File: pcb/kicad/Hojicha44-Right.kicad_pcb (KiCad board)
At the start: 2 copper layers, 150.5 x 114.6 mm, 54 parts

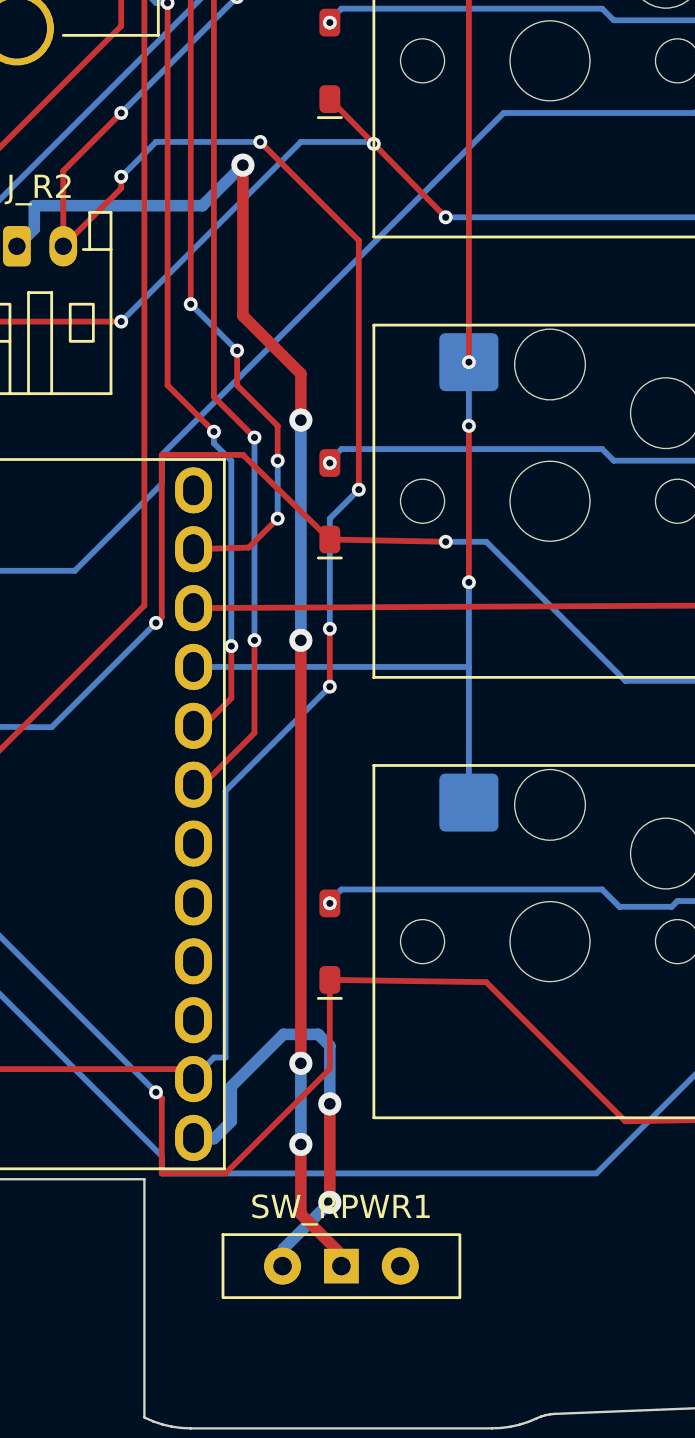
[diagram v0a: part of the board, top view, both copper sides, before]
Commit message: Review round 2: B1 pillar clearance blocker + T4 cover magnets + M2 pwrsw shift + M1 floor ruler + gate hardening
B1 (blocker): tab pillar fuse reached 1.0mm inboard of the rim - solid
case material under the PCB at all 8 stations (board rests ~1.05mm
high, bottom pads unload). Pillar now starts 0.3 outboard of the rim;
new gates: per-tab footprint-clear probes + plan-wide PCB-rim sweep
at z=-1.0. First attempt (fuse deletion) was wrong - the gates caught
it: the tab lobes are cavity in the v3.1 dilation, the fuse IS the
shelf. Tub 68.0 -> 67.4 cm3.

T4: cover magnets 04x1.5 (16 pcs, pocket 1.7, floor 0.8 -> 1.3mm);
faces still meet at the lip plane; BOM rows added (magnets were
missing entirely); first-article pull test >=1.5 kg.

M2: pwrsw footprint 2mm west (ergogen [9,14]->[7,14]) so the blade
band sits under the SAT-constrained mouth window. Left stub endpoints
moved; Right's 31 stale hand-routed pwrsw items deleted (router
re-routes fresh). Router: obstacle model seeded with preserved GUI
copper at exact clearance (MARGIN-inflated seed rejected the legal
COL5_R corridor); copper checker sees merged board with dangle
reporting scoped to preserved items; co-located router/GUI vias
deduped. DRC both halves clean (W1 set only).

M1: floor derivation rewritten to the measured below-PCB ruler
(encoder legs -3.65 from the vendored STEP - deepest; sockets are
top-side and never provisioned the floor). FLOOR_Z -5.6 keeps
~1.95mm - no geometry change.

M6/M7/M8: gen_cover in CI; stack-ties in spec_checks.cjs; pwrsw in
plate tab eligibility (DXFs byte-identical); definitive encoder web
print (cutouts 9.15 / windows 3.65 / ports 4.92-5.35).

H1: Choc 15.0 kept with honest wording (lower body 13.8, clips never
engage at 15.0/1.5mm - coherent with the plate; rev-2 coupon decides).
LOW doc cluster: TRRS chord 6.42-at-lip, encoder 24.04 shaft-center
rationale, HISTORICAL annotations on pre-fix rows, DXF layer docstring
PORON, v3.4 changelog axis 2.4->2.5 noted.
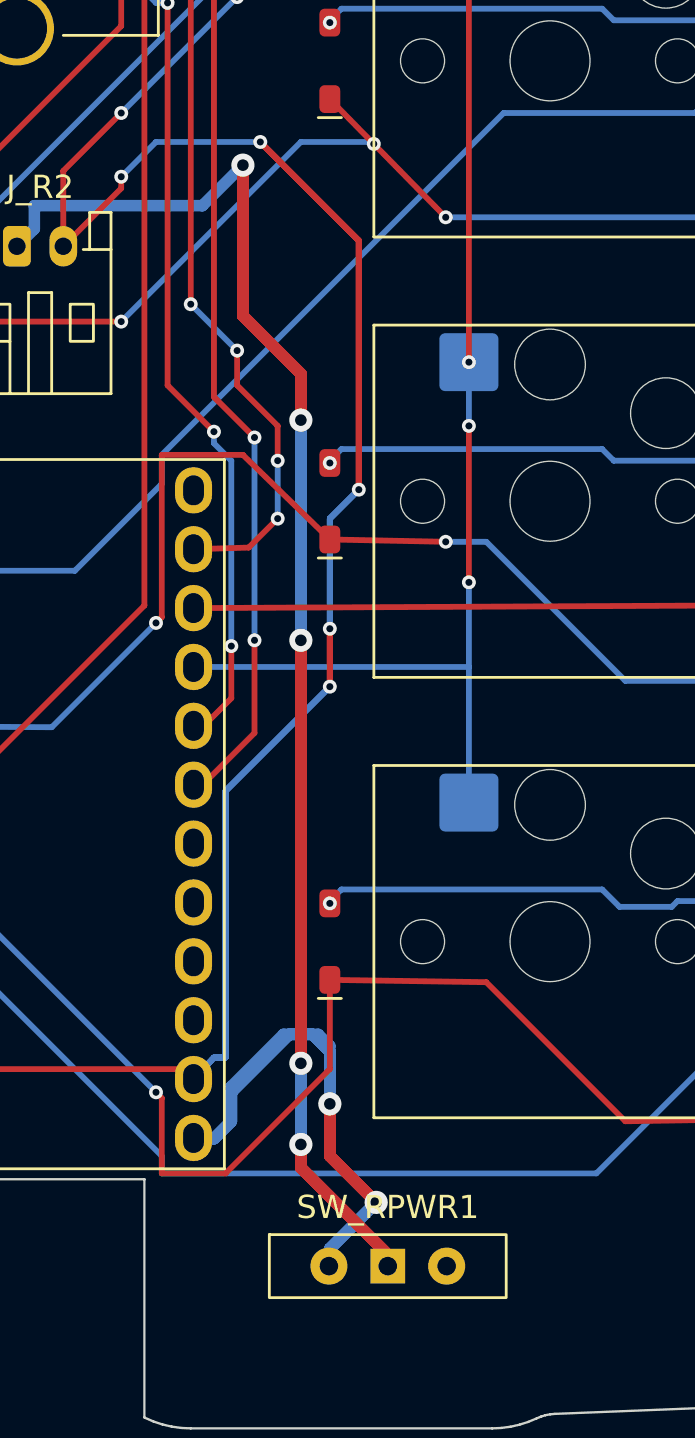
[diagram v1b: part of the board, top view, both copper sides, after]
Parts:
- moved SW_RPWR1 2.00 mm to (189.5, 51.0)
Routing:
- net GND: track 156.8 -> 293.0 mm
- net Net-(J_R2-Pin_1): track 61.0 -> 161.1 mm
- net /VBAT_SW_R: track 19.2 -> 59.4 mm

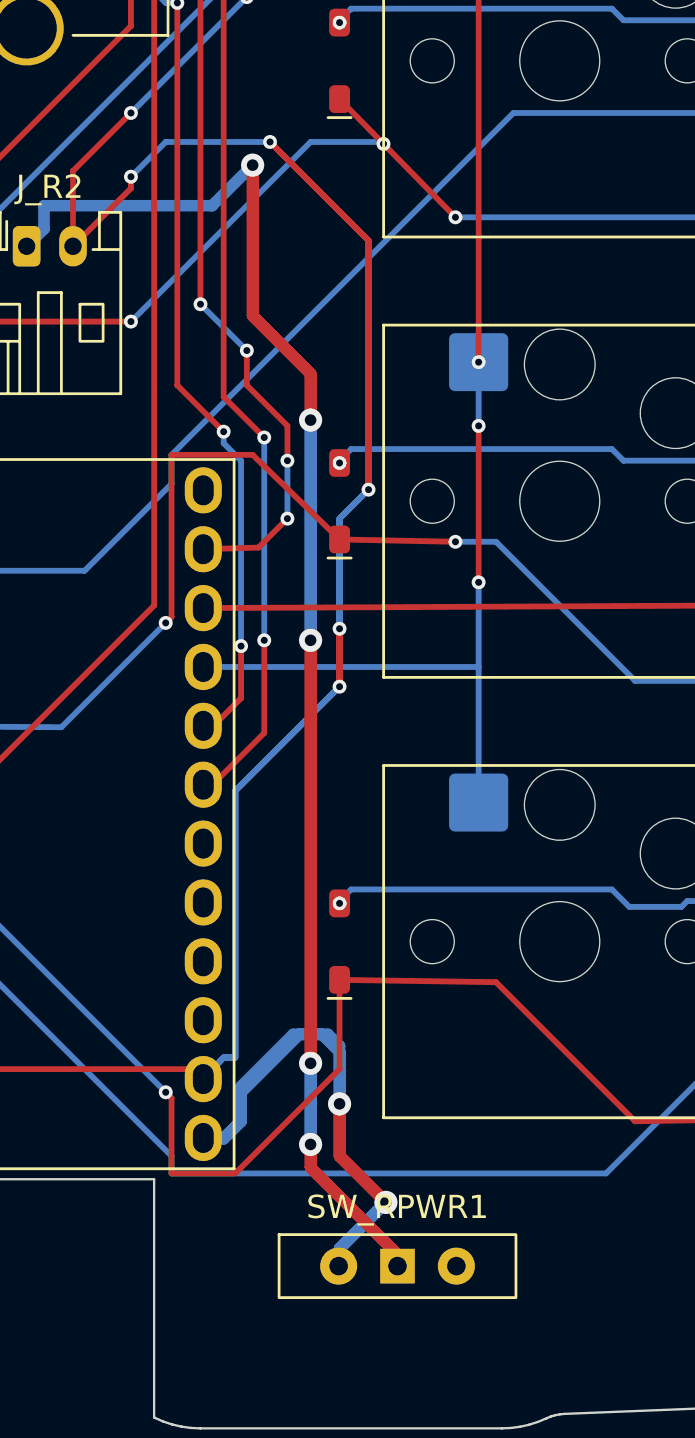
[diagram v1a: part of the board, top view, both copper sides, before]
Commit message: M3: recentre pwrsw to SAT window centres 106.3/185.2 — plateau frozen to committed Edge.Cuts, routes regenerated (nets 20/45 router-owned, silk ref_shift mirrored)
Multi-model datasheet verification overturned the M2 offset reading; the
switch is now centred on the SAT-pinned window on both halves (mirror-exact
about x=145.75). Window tracks the switch via ergogen pwrsw shift 11.3;
plateau decoupled and frozen so frame stays axis-exact. Gates: gen_pcb exit
0, DRC 28 x W1-waived per half only, ERC 0 err / 5 spare warns per half,
topology 0 dangling, npm test green, plate --check CLEAN, case+cover
regenerated with census green. Switch body 101.3..111.3, lever band
0.70/side vs window - was 4.3 mm outboard with zero visible blade.
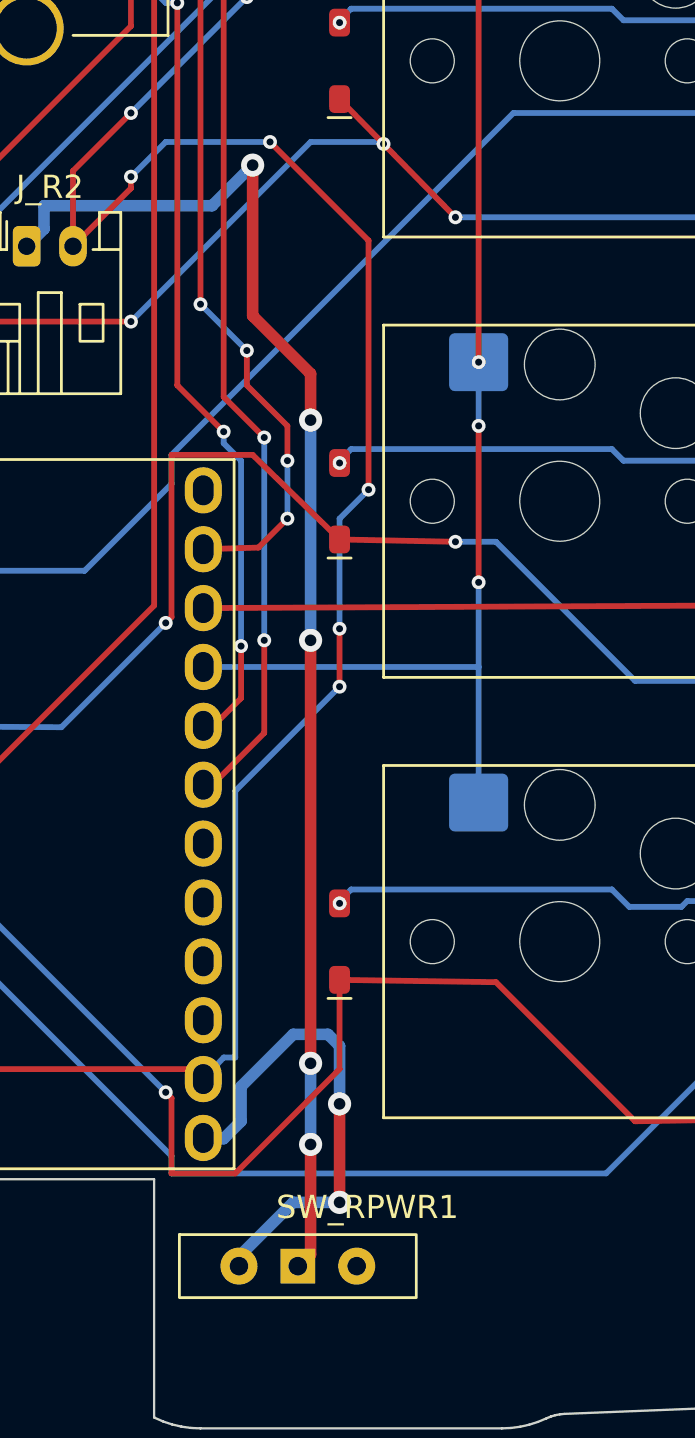
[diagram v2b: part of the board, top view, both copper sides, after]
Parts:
- moved SW_RPWR1 4.30 mm to (185.2, 51.0)
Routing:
- net GND: track 293.0 -> 156.8 mm
- net Net-(J_R2-Pin_1): track 161.1 -> 60.6 mm
- net /VBAT_SW_R: track 59.4 -> 21.3 mm

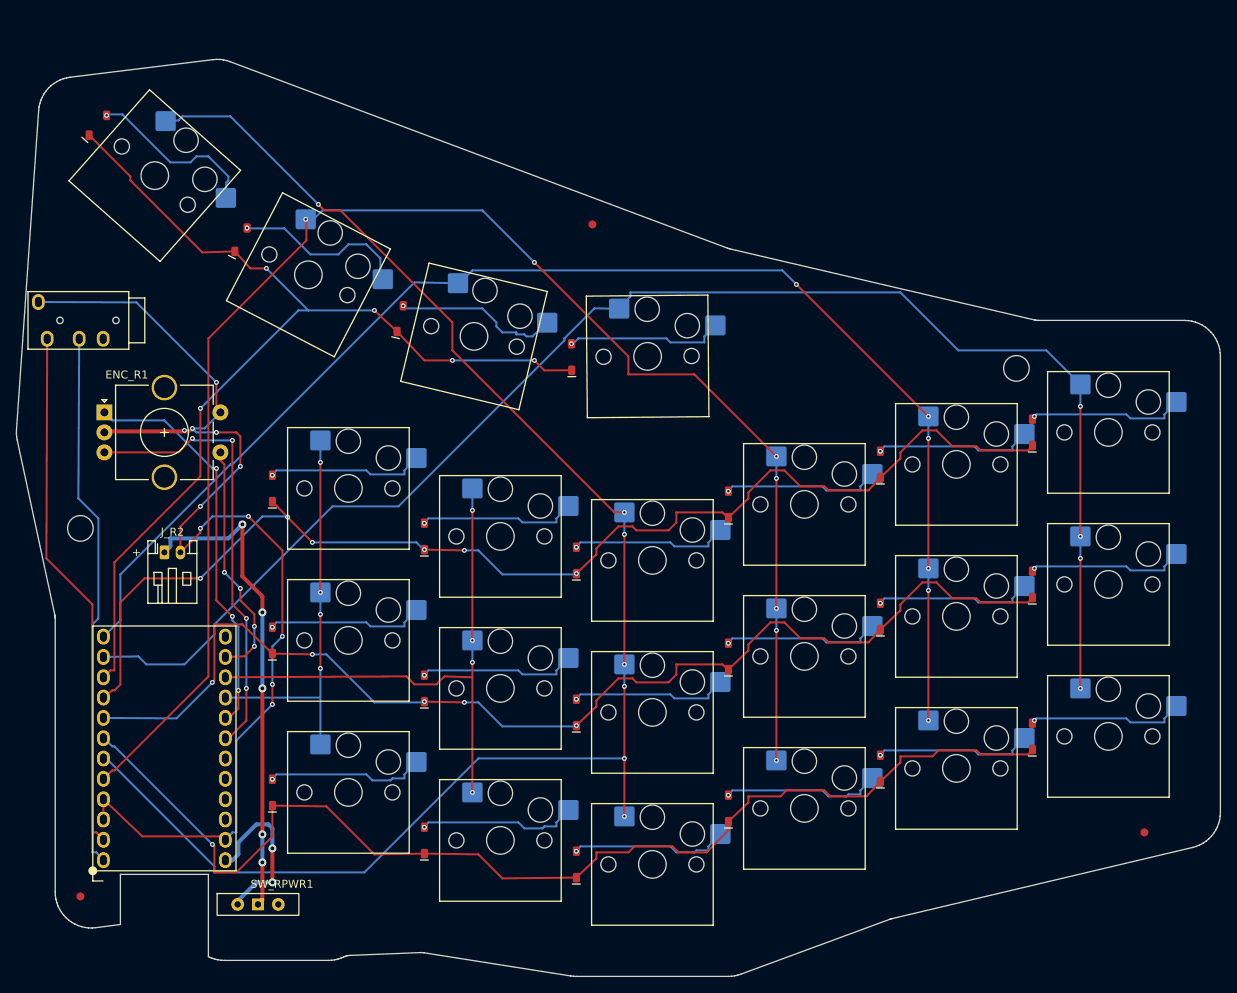
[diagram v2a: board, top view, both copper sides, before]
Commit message: M3.1: post-audit P0 batch + provenance pipeline
- gen_pcb: pcb/kicad/hand-copper.txt manifest replaces the
  classify-by-reproduction heuristic (phase-1 deleted; extraction reads
  the committed baseline via git HEAD; copper gates before write; a
  DRC-rejected board is archived + reverted so it never feeds the next
  build). Idempotency proven: three consecutive regens byte-identical
  modulo uuid/date, DRC clean (28 W1-waived only); Left corridor
  regenerated fresh and converged (the 6 stale corridor items were
  router-owned; frozen they pinned a 1.0607mm via collision).
- gen_route: via rules from this round stand — signal pads 0.60->0.65
  (annular), same-net pairs keep the drill rule, cross-net pairs use
  the pad rule, later nets yield to earlier vias; ROUTER_VERSION r13.
- gen_schematic: POWER netclass patterns; ERC 0 errors.
- plate: USB-plug bay floor scan re-anchored on the config usb mouth
  (band-min grabbed the west-edge outline); all plate gates CLEAN.
- case: P0 magnet policy (pocket 4.3, web 1.15, band 6.6) now backed
  by CASE_OUTSET 7.0->7.1 — physical band 6.5->6.6 exactly; stations
  6/7, wall_min 1.60; cover reuses the tub scan (web 1.15).
- keymap: right thumbs RSFT/RALT/mo2/ENTER, right inner BSLH/RBKT/ESC,
  3rd layer raise_layer; spec_checks derives the 46-position list from
  layout.yaml; layout.yaml open_points drops the resolved chord item.
- make_release: dirty-tree refusal + ERC/DRC report gating + ENIG
  stamp; checks.yml board_gates job; doc sweeps (README, case/README,
  spec/case.md, notes.md 2026-10-19 section).
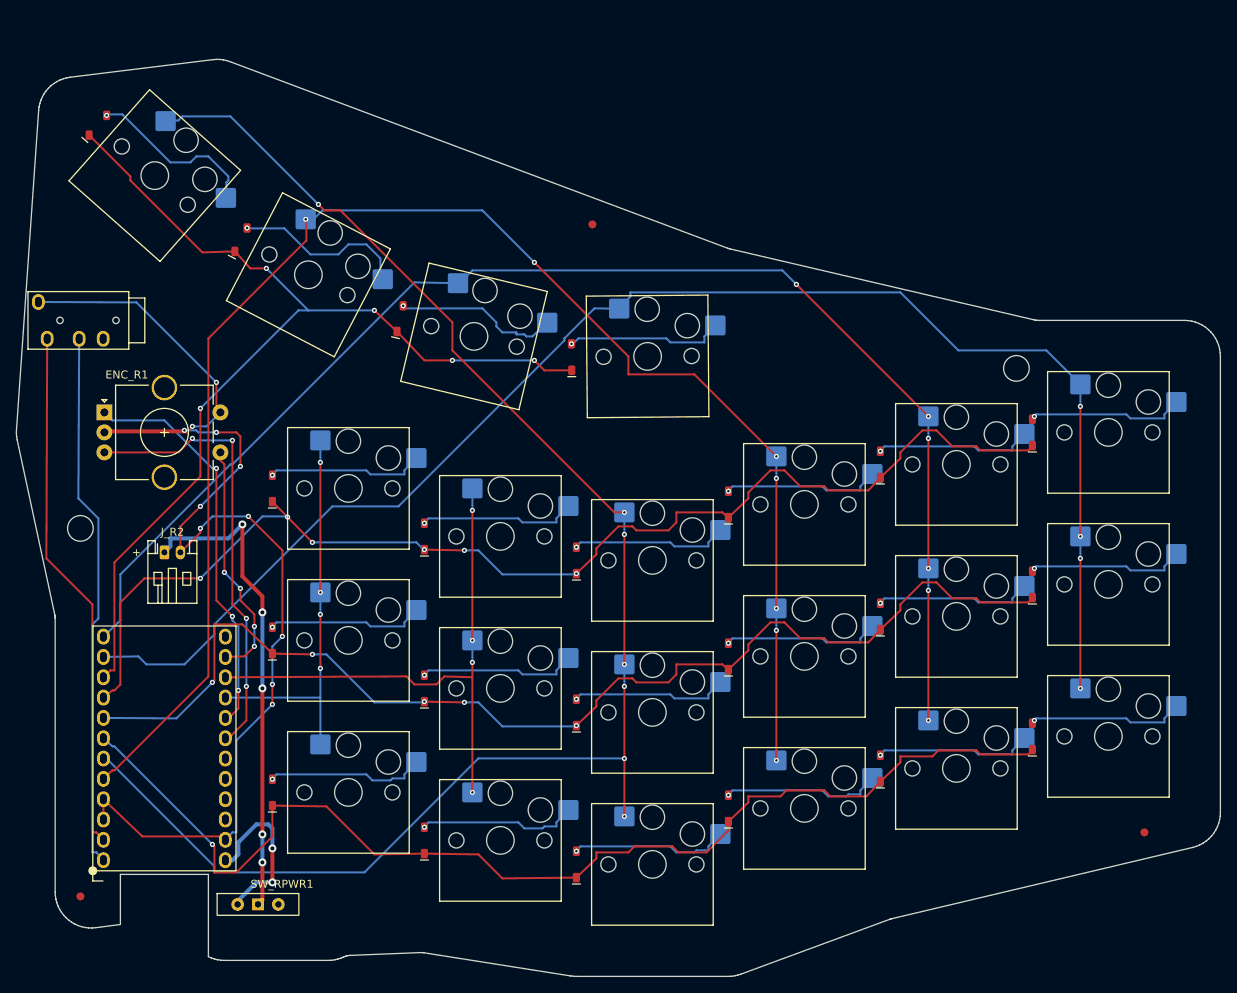
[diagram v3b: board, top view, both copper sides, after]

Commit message: frame: store board y-negated so releases match plate; gate it
KiCad's Gerber/drill/pos writers negate stored y.  The board was stored
in the plate/case design frame, so every release was the Y-mirror of the
plate: T12 centres landed on the mirror of the cutouts and the T10 switch
posts were handed the wrong way (a standard Choc could not install).

- add pcb/generators/frame.py: full board reflection (global + footprint
  local geometry/angles), title-block frame marker, idempotent readers
- gen_pcb builds in design frame and reflects at the write boundary
- plate/case/check_board readers convert storage -> design
- check_board: cross-artifact frame gate (T12 centres, T10 post
  handedness, USB-notch outline) with Y-negated negative controls
- DRC runs on the design-frame reflection with a matching project copy
  (the storage frame would flag all 54 footprints as library mismatches)
- make_release: full SHA-256 manifest digests + board-byte verification
- quarantine the stale pcb/- FINAL tree; bump spec to 0.4.0
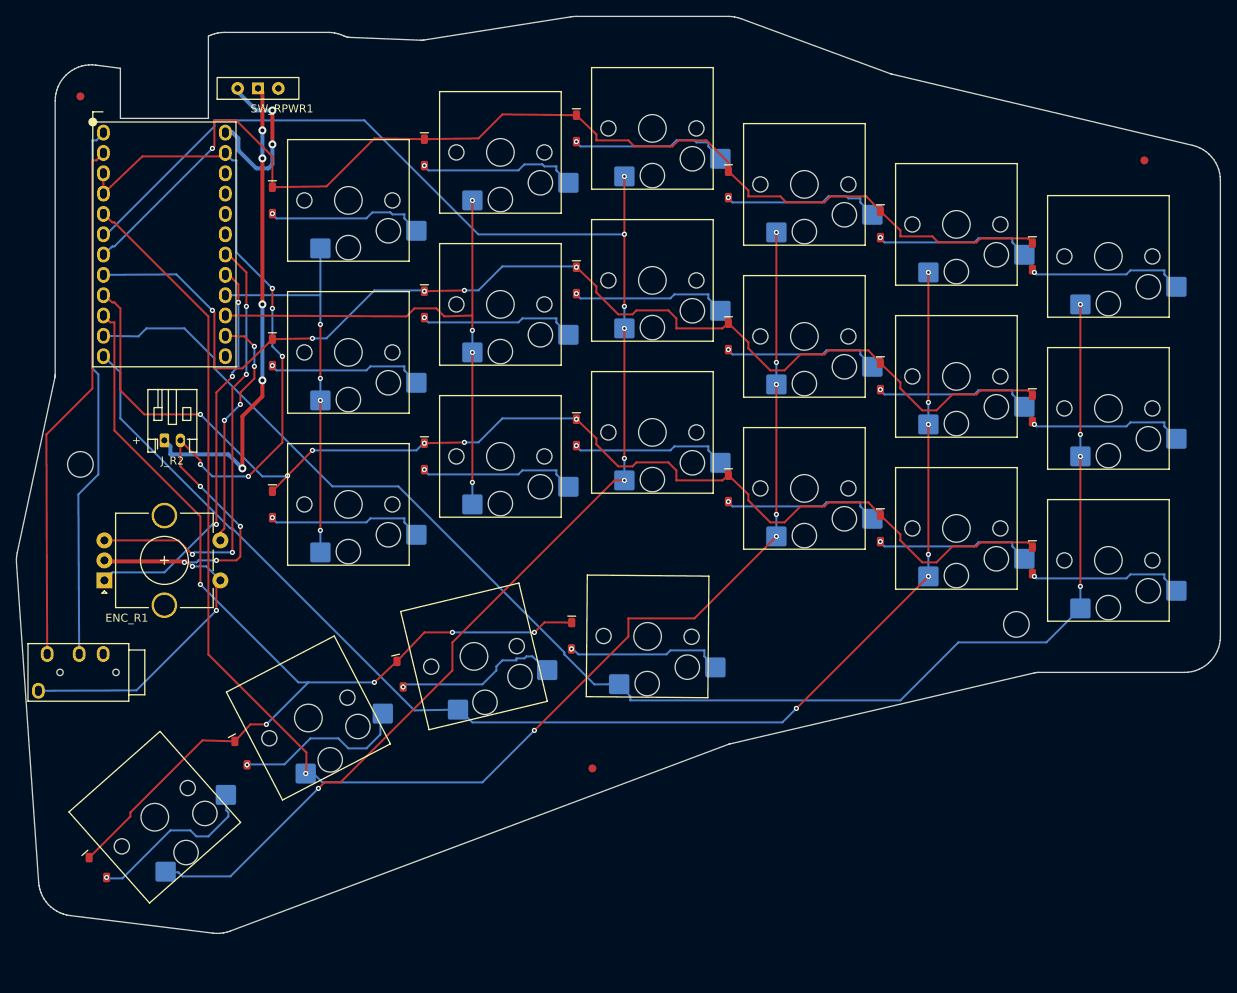
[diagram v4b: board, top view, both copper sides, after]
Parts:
- moved SW_RPWR1 102.0 mm to (185.2, -51.0)
- moved FID_R1 100.0 mm to (163.0, -50.0)
- moved D_R21 92.8 mm to (165.2, 46.4), turned to -48.5 degrees
- moved D_R03 92.0 mm to (225.0, -46.0), turned to -90 degrees
- moved SW_R03 92.0 mm to (234.5, -46.0)
- moved U_R1 90.9 mm to (165.9, -45.5)
- moved D_R04 86.0 mm to (206.0, -43.0), turned to -90 degrees
- moved SW_R04 86.0 mm to (215.5, -43.0)
- moved FID_R2 84.0 mm to (296.0, -42.0)
- moved SW_R21 80.2 mm to (172.3, 40.1), turned to 41.5 degrees
- moved D_R02 78.0 mm to (244.0, -39.0), turned to -90 degrees
- moved SW_R02 78.0 mm to (253.5, -39.0)
- moved D_R05 74.0 mm to (187.0, -37.0), turned to -90 degrees
- moved SW_R05 74.0 mm to (196.5, -37.0)
- moved D_R01 68.0 mm to (263.0, -34.0), turned to -90 degrees
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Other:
- outline, holes or cut-outs redrawn
